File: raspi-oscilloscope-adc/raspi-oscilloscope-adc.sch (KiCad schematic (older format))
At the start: 25 parts, among them J1 Conn_Coaxial, J2 Conn_01x10_Male, J3 Conn_01x02_Male, SW1 SR10010F-0106-20F0B-C7-N-0027, U1 ECS-220B-100, U2 TLC5510INSR, U3 OPA690

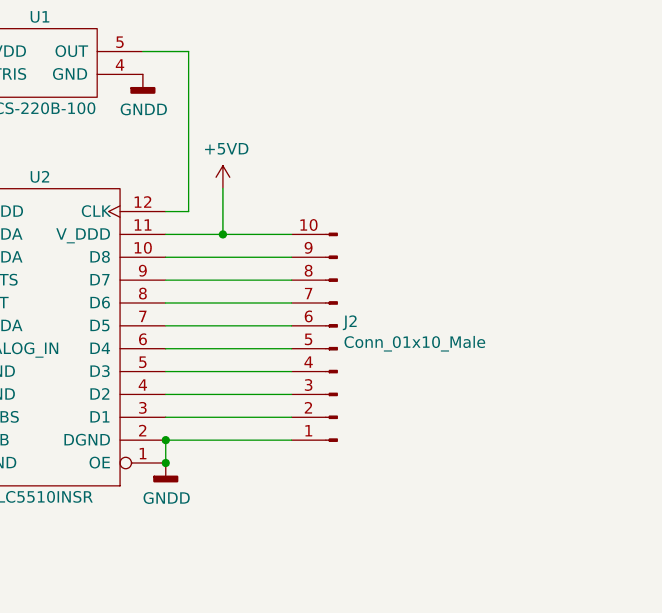
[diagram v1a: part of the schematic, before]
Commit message: Add 5V to 3V3 logic converter
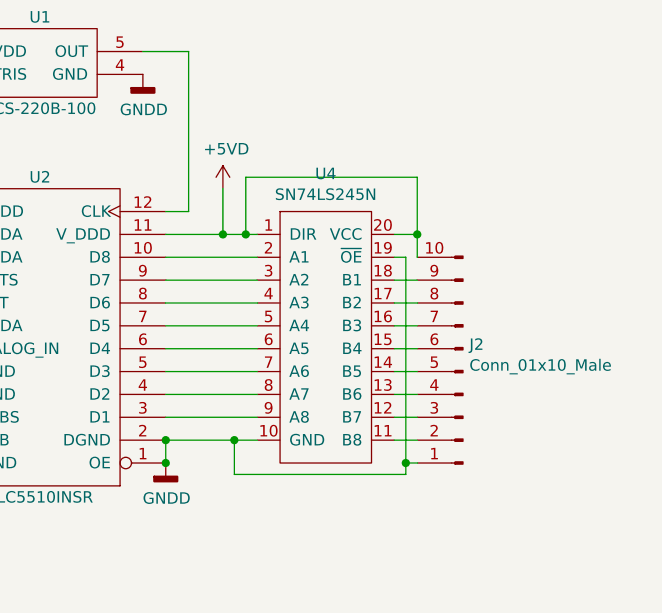
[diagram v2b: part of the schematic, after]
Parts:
- added U4: SN74LS245N, Package_DIP:DIP-20_W7.62mm, symbol Interface:SN74LS245N
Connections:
- net +5VD: now also U4.1 (DIR), U4.20 (VCC)
- net GNDD: now also U4.10 (GND), U4.19 (~OE)
- net at U2.10 (D8): now also U4.2 (A1); no longer J2.9 (Pin_9)
- net at U2.3 (D1): now also U4.9 (A8); no longer J2.2 (Pin_2)
- net at U2.4 (D2): now also U4.8 (A7); no longer J2.3 (Pin_3)
- net at U2.5 (D3): now also U4.7 (A6); no longer J2.4 (Pin_4)
- net at U2.6 (D4): now also U4.6 (A5); no longer J2.5 (Pin_5)
- net at U2.7 (D5): now also U4.5 (A4); no longer J2.6 (Pin_6)
- net at U2.8 (D6): now also U4.4 (A3); no longer J2.7 (Pin_7)
- net at U2.9 (D7): now also U4.3 (A2); no longer J2.8 (Pin_8)
- new net: J2.2 (Pin_2), U4.11 (B8)
- new net: J2.3 (Pin_3), U4.12 (B7)
- new net: J2.4 (Pin_4), U4.13 (B6)
- new net: J2.5 (Pin_5), U4.14 (B5)
- new net: J2.6 (Pin_6), U4.15 (B4)
- new net: J2.7 (Pin_7), U4.16 (B3)
- new net: J2.8 (Pin_8), U4.17 (B2)
- new net: J2.9 (Pin_9), U4.18 (B1)
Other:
- moved on the sheet: J2
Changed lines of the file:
@@
 $EndComp
 Wire Wire Line
-	8000 3650 7450 3650
-Wire Wire Line
-	7450 3750 8000 3750
-Wire Wire Line
-	8000 3850 7450 3850
-Wire Wire Line
-	7450 3950 8000 3950
-Wire Wire Line
-	8000 4050 7450 4050
-Wire Wire Line
-	7450 4150 8000 4150
-Wire Wire Line
-	7450 4250 8000 4250
-Wire Wire Line
-	7450 4350 8000 4350
+	7450 3750 7850 3750
 $Comp
 L Connector:Conn_Coaxial J1
@@
 L Connector:Conn_01x10_Male J2
 U 1 1 5EFDEB4A
-P 8200 4050
-F 0 "J2" H 8172 3932 50  0000 R CNN
-F 1 "Conn_01x10_Male" H 8172 4023 50  0000 R CNN
-F 2 "Connector_PinHeader_2.54mm:PinHeader_1x10_P2.54mm_Vertical" H 8200 4050 50  0001 C CNN
-F 3 "~" H 8200 4050 50  0001 C CNN
-	1    8200 4050
+P 8750 4150
+F 0 "J2" H 8722 4032 50  0000 R CNN
+F 1 "Conn_01x10_Male" H 8722 4123 50  0000 R CNN
+F 2 "Connector_PinHeader_2.54mm:PinHeader_1x10_P2.54mm_Vertical" H 8750 4150 50  0001 C CNN
+F 3 "~" H 8750 4150 50  0001 C CNN
+	1    8750 4150
 	-1   0    0    1
 $EndComp
-Wire Wire Line
-	7450 4450 8000 4450
 Connection ~ 7450 4450
-Wire Wire Line
-	8000 3550 7700 3550
 Connection ~ 7700 3550
 $Comp
@@
 NoConn ~ 4800 4750
 NoConn ~ 4800 4850
+Wire Wire Line
+	7850 3550 7800 3550
+Wire Wire Line
+	7850 3650 7450 3650
+Wire Wire Line
+	7850 3850 7450 3850
+Wire Wire Line
+	7450 4350 7850 4350
+Wire Wire Line
+	7450 4250 7850 4250
+Wire Wire Line
+	7450 4150 7850 4150
+Wire Wire Line
+	7850 4050 7450 4050
+Wire Wire Line
+	7450 3950 7850 3950
+Wire Wire Line
+	7450 4450 7750 4450
+$Comp
+L Interface:SN74LS245N U4
+U 1 1 5EFAA0A7
+P 8150 4000
+F 0 "U4" H 8150 4715 50  0000 C CNN
+F 1 "SN74LS245N" H 8150 4624 50  0000 C CNN
+F 2 "Package_DIP:DIP-20_W7.62mm" H 8150 4100 50  0001 C CNN
+F 3 "" H 8150 4100 50  0001 C CNN
+	1    8150 4000
+	1    0    0    -1
+$EndComp
+Wire Wire Line
+	7750 4450 7750 4600
+Connection ~ 7750 4450
+Wire Wire Line
+	7750 4450 7850 4450
+Wire Wire Line
+	8450 4450 8550 4450
+Wire Wire Line
+	8550 4350 8450 4350
+Wire Wire Line
+	8450 4250 8550 4250
+Wire Wire Line
+	8450 4150 8550 4150
+Wire Wire Line
+	8450 4050 8550 4050
+Wire Wire Line
+	8450 3950 8550 3950
+Wire Wire Line
+	8450 3850 8550 3850
+Wire Wire Line
+	8450 3750 8550 3750
+Wire Wire Line
+	8550 3650 8550 3550
+Wire Wire Line
+	8550 3550 8450 3550
+Wire Wire Line
+	7800 3550 7800 3300
+Wire Wire Line
+	7800 3300 8550 3300
+Wire Wire Line
+	8550 3300 8550 3550
+Connection ~ 7800 3550
+Wire Wire Line
+	7800 3550 7700 3550
+Connection ~ 8550 3550
+Wire Wire Line
+	8500 4600 8500 4550
+Wire Wire Line
+	8500 3650 8450 3650
+Wire Wire Line
+	8550 4550 8500 4550
+Connection ~ 8500 4550
+Wire Wire Line
+	8500 4550 8500 3650
+Wire Wire Line
+	8500 4600 7750 4600
 $EndSCHEMATC
